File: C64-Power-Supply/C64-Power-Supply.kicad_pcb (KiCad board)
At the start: 2 copper layers, 139.7 x 78.1 mm, 18 parts, among them J1 PWR_IN, J2 V_Select, J3 Conn_01x07, T1 Transformer_2P_2S

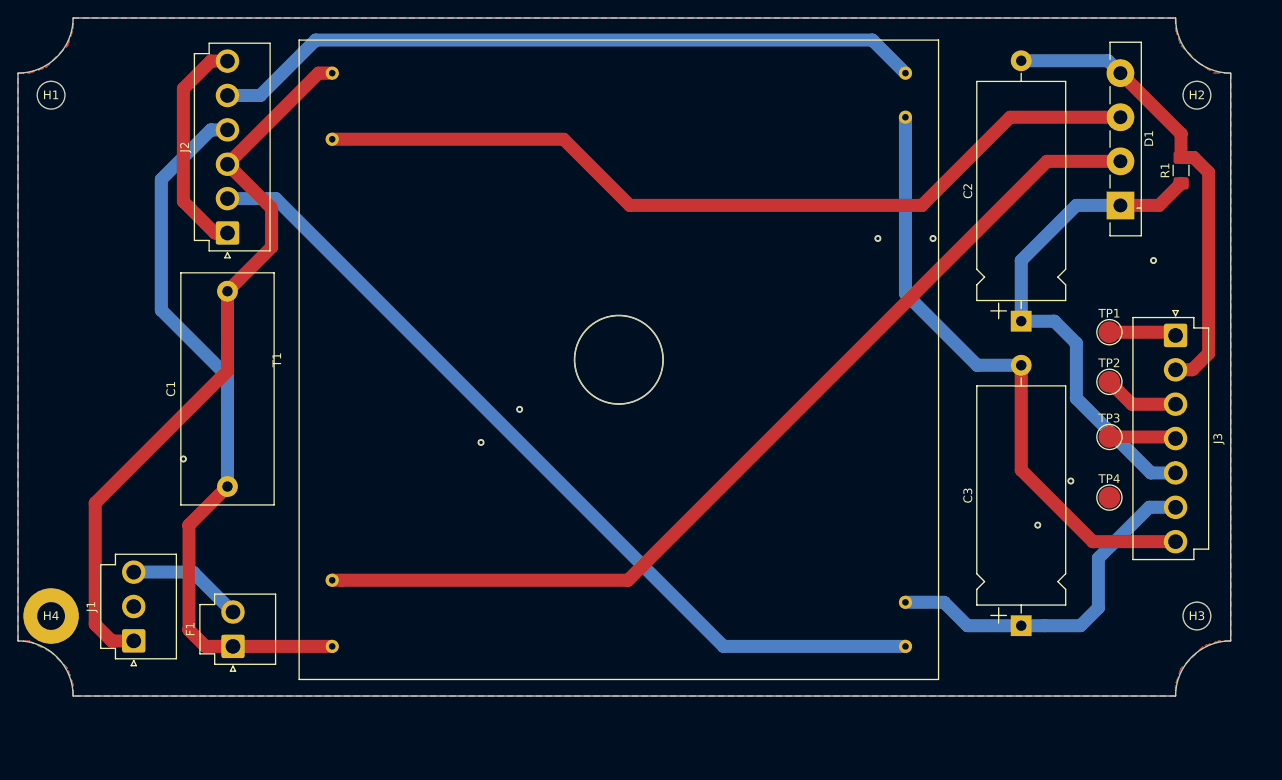
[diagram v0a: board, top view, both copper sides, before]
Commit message: Added 5VDC regulation
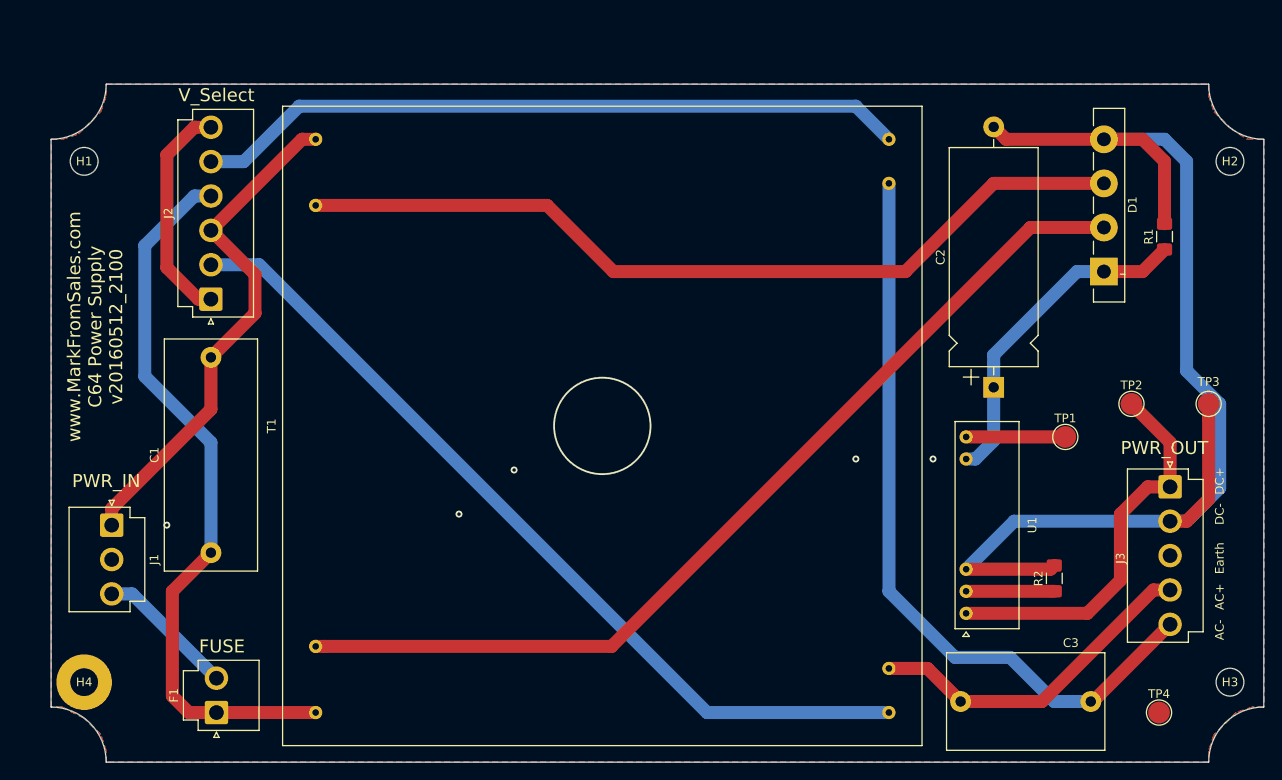
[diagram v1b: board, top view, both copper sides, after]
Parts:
- added R2: 1.472K, Resistor_SMD:R_1206_3216Metric_Pad1.42x1.75mm_HandSolder, F.Cu at (191.8, 106.5)
- added U1: AXA003A0XZ, MarkFromSales:AXA003A0XZ, F.Cu at (181.6, 100.3)
- C3: value 50u -> 1uF 25VAC; footprint Capacitor_THT:CP_Axial_L25.0mm_D10.0mm_P30.00mm_Horizontal -> Capacitor_THT:C_Rect_L18.0mm_W11.0mm_P15.00mm_FKS3_FKP3
- J3: value Conn_01x07 -> PWR_OUT; footprint Connector_JST:JST_VH_B7P-VH_1x07_P3.96mm_Vertical -> Connector_JST:JST_VH_B5P-VH_1x05_P3.96mm_Vertical
- moved TP4 25.4 mm to (203.8, 121.9)
- moved J3 17.5 mm to (205.1, 95.9)
- moved J1 13.6 mm to (83.2, 100.3), turned to 270 degrees
- moved TP1 13.1 mm to (193.0, 90.2)
- moved TP3 12.0 mm to (209.6, 86.4)
- moved C3 11.2 mm to (181.0, 120.7), turned to 0 degrees
- moved H1 8.52 mm to (80.0, 58.4)
- moved H2 8.52 mm to (212.0, 58.4)
- moved H3 8.52 mm to (212.0, 118.4)
- moved H4 8.52 mm to (80.0, 118.4)
- moved C2 8.26 mm to (184.8, 84.5)
- moved F1 7.85 mm to (95.2, 121.9)
- moved J2 7.85 mm to (94.6, 74.3)
- moved R1 7.85 mm to (204.5, 67.1)
- moved T1 7.85 mm to (139.7, 88.9)
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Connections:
- J3 pad 3: Net-(J3-Pad3) -> Earth
- J3 pad 4: Net-(J3-Pad4) -> Net-(C3-Pad1)
- J3 pad 5: Net-(C2-Pad1) -> Net-(C3-Pad2)
- TP1 pad 1: Net-(J3-Pad1) -> Net-(TP1-Pad1)
- TP2 pad 1: Net-(J3-Pad3) -> Net-(J3-Pad1)
- TP3 pad 1: Net-(J3-Pad4) -> Net-(C2-Pad2)
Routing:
- net Net-(C2-Pad2): track 54.0 -> 138.2 mm
- net Net-(J3-Pad1): track 7.77 -> 45.4 mm
- net Net-(C1-Pad2): track 85.2 -> 59.3 mm
- net Net-(C2-Pad1): track 57.8 -> 38.6 mm
- net Net-(C3-Pad2): track 70.3 -> 88.3 mm
- net Net-(TP1-Pad1): track 0.00 -> 11.4 mm
- net Net-(R2-Pad1): track 0.00 -> 10.2 mm
- net Net-(J3-Pad3): track 8.69 -> 0.00 mm
- net Net-(J3-Pad4): track 7.70 -> 0.00 mm
- net Net-(F1-Pad2): track 13.3 -> 16.1 mm
- net Net-(C3-Pad1): track 41.2 -> 39.3 mm
- net Earth: vias 8 -> 5
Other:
- outline, holes or cut-outs redrawn
- board text added: "AC+"
- board text added: "AC-"
- board text added: "DC+"
- board text added: "DC-"
- board text added: "Earth"
- board text added: "FUSE"
- board text added: "PWR_IN"
- board text added: "PWR_OUT"
- board text added: "V_Select"
- board text added: "www.MarkFromSales.com C64 Power Supply v20160512_2100"
